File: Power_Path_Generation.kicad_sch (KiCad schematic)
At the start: 8 parts, among them Q602 PMOS SI2365EDS-T1-GE3, U701 TPS7A0233DQNR, U702 TPS3839G33DQNR

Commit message: Added footprints, images, almost finished all èages except for the MCU
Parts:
- added TP701: COUT, 0_Zenith:TestPoint_Pad_D0.5mm_Front, symbol Connector:TestPoint
- added TP702: DOUT, 0_Zenith:TestPoint_Pad_D0.5mm_Front, symbol Connector:TestPoint
- added TP703: -VBAT, 0_Zenith:TestPoint_Pad_D0.5mm_Front, symbol Connector:TestPoint
- added TP704: VBAT, 0_Zenith:TestPoint_Pad_D0.5mm_Front, symbol Connector:TestPoint
- renumbered C616 to C701, C614 to C702, C615 to C703, D602 to D701, Q602 to Q701, R607 to R701, U702 to U701, U701 to U702
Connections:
- net +VBAT: now also TP704.1
- new net -VBAT: TP703.1
- new net COUT: TP701.1
- new net DOUT: TP702.1

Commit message: Added RGB LED, added motor connectors, added test points, imported all 3D models
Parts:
- TP701, TP702, TP703, TP704: footprint 0_Zenith:TestPoint_Pad_D0.5mm_Front -> 0_Plume:TestPoint_Pad_D0.5mm_Back
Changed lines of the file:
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@@
 			"AAAAAAAAAAAAAAAAAAAAAAAAAAAAAAAAAAAAAAAAAAAAAAAAAAAAAAAAAAAAAAAAAAAAAAAAAAAA"
 			"AAAAAAAAAAAAAAAAAAAAAAAAAAAAAAAAAAAAAAAAAAAAAAAAAAAAAAAAAAAAAAAAAAAAAAAAAAAA"
-			"AAAAAAAAAAAAAAAAAAAAAAAAAAAAAAAAAAAAAAAAAAAAAAAAAAAAAAAAAA=="
+			"AAAAAAAAAAAAAAAAAAAAAAAAAAAAAAAAAAAAAAAAAAAAAAAAAAAAAAAAAP//////////////////"
+			"////////////////////////////////////////////////////////////////////////////"
+			"////////////////////////////////////////////////////////////////////////////"
+			"////////////////////////////////////////////////////////////////////////////"
+			"////////////////////////////////////////////////////////////////////////////"
+			"////////////////////////////////////////////////////////////////////////////"
+			"///////////////////////////////+/v7//f39//z8/P/7+/v//Pz8//39/f/+/v7/////////"
+			"///+/v7//Pz8//j3+P/z8/P/7+/v/+fn5//c3Nz/0NDQ/8LCwv+5ubn/tbW1/7Gxsf+tra3/rKys"
+			"/6ysrP+srKz/q6ur/6urq/+rq6v/rKys/62trf+urq7/r6+v/7Gxsf+zs7P/tbW1/7a2tv+4uLj/"
+			"uru5/7y9uv+/v73/wcG//8TDwf/FxML/xsTD/8fGxP/Jx8X/ysjG/8rIxv/JyMb/yMjH/8jIyP/J"
+			"ycn/ycnJ/8rKyv/Ly8v/y8vL/8vLy//My8z/zMzM/8zMzP/MzMz/zc3N/87Ozv/Ozs7/zs7O/87O"
+			"zv/Pz8//z8/P/8/Pz//Pz8//z8/P/8/Pz//Q0ND/0tLR/9PT0f/T09H/09PR/9TU0v/U1NL/1NTS"
+			"/9TU0v/V1dP/1dXT/9XW1P/W19T/1tfU/9bX1P/X19X/19fV/9jX1f/Z19X/2dfV/9nX1f/Z19X/"
+			"2dfV/9nX1f/Z19X/2dfW/9nY1//a2Nf/2tnX/9vZ2P/c2tn/3t3b/97d2//c2tn/2tnX/9nY1v/a"
+			"2Nf/3NvZ/+Df3f/m5eP/5eTi/97d2//g3t3/6ujn/+/t6//v7ev/6ujn/+De3f/Qz87/urq6/6Gh"
+			"of+EhIT/cHBw/2RkZP9bW1v/VVRV/1BQUP9NTU3/SEhI/0NDQ/88PDz/NTU1/zAwMP8vLy//Ly8v"
+			"/zAwMP8wMDD/Ly8v/y8vL/8wMDD/MjIy/zMzM/8zMzP/MjIy/zIyMv8zMzP/MTEx/ywsLP9TU1P/"
+			"qKio/97e3v/09PT//////////////////////////////////v7+//z8/P/7+/v//f39//39/f/9"
+			"/f3//Pz8//n5+f/39/f/9vb2//j4+P/9/f3//v7+//z8/P/4+Pj/8vLy/w=="
 		)
 	)
@@
 			"LoguiC6ILoguiC6ILoguiC6ILoguiC6ILoguiC6ILoguiC6ILoguiC6ILoguiC6ILoguiC6ILogu"
 			"iC6ILoguiC6ILoguiC6ILoguiC6ILoguiC6ILoguiC6ILoguiC6ILoguiC6ILoguiC6ILoguiC6I"
-			"LoguiC6ILg=="
+			"LoguiC6ILmdrQkI0RU5Hb0JBMEgvSUNsT0VMQWdXQmdrQkJvQ0JRRVBqTkkvRDY2Njl2ZnZXTFg2"
+			"MlRaRnRkZmdTM25nbThQQWJVdzFXOEl5TlFKZ2NZUHZSZDJSdXVxVWpySmlUSnNrNUdKeFY1Q1JI"
+			"VFlFc0dKRkloS2U5WjRjOWtSZXp0UjhzVytzbjNIVk1GVzJWYUY2TmVDQm9KRllQQXJ1UG1ZdERn"
+			"bGVVVjNGNVEyRGVvRjdwNElpRkNPVWQ0KzFJMmxmYm9sM0VzV3N6MEU5OW1pTGdsSTJTQ0dwK2Nx"
+			"SVpHSkduNklXY0dPU2JHRFh1RHp0cngwdkpTdEF2RlBvNTJMVUNVMlRvcDVYTWFRTm5kckIveGRk"
+			"ZzdmaVl6N0NMZEYwZGNlaUFXeE11TVE5WUx2Sml6NmJHcEVWamJKcy9INDBReVpLS25OVEZ2VUx6"
+			"bldOR1gvYkZKZ0hnOWo1dHFwdGZjbDFoWjl4ZVZ2RjRKejdRdVhyTytzWUVjTDlmeE9JOGZKQjVy"
+			"a2ViQlhJS2tjc0hCaExscEhXT21KaTFsRFBTOHZiMFo4V2FZUG11cnRjdzZxZEVoWmdqOGJOd1pD"
+			"Ym91cktwMGUzSXVYVjNkUWFaMXM5Y0NKOFdYb1gvV1BEOC9ES01kV013L3oxVzVEVmlzZk1pcTFj"
+			"dzYyeTNPejJESmRCU0JYMGVFRjNIOWU2R3J2bmJ5NDUvN281bS8vdXUvM3REaTdCZmhVNjRWQkFv"
+			"Q0JZR0N3SWVEUUNGb1BoemN5NmdGZ1lKQVFhQWdVQkFvQ1B5V0VUaHd6NEUxVWxjM1VZN0hjVU81"
+			"RjkxMXJMbmRNT29xaHlpNDZ1NVlkYWloUm9CWktwS2lHMFdadXdSemJhSnNhMEZqTmlVVmFlTjRZ"
+			"TVBTSWdhaWNjeEFKVGtyODNFTVNhR3lyYkljbmJQM3Vwc1hhdHp2Nm1xRHBDRW9NR1NBS2JrTkJs"
+			"ekhhb2JzeS9TVm1rbG8yTUsrM2JjVHhOaEM5ZWhmeTR3ZU1rTU5RTVJNUU1yc083QS9YS2Q2K2tu"
+			"UmpCdFZiMThYcEV4dnVGUkpCT25hdE1rOFZuQ3JNU2FPL2FybzZ5NmtXNUlVUThUT1lZd2RXYm5H"
+			"U2NUVENWY2ZaQTh5UUptNDdqdzlUMXVTTlpFbUNPbWNhYTRMa05mU3JKeEp4c3ZqMURhTlo1TkV4"
+			"aWhieHBSSzBYOTJRY3JucWMrRWhmMGtlYlJ5U3ZYei9keTN5eUhoNGZqZVM2NVlpZlRhV3plVE5z"
+			"N0o2MGlvWUR2WStDeHdoWHZlWjExNFZqbzZKSTNzczZwR0ljZEd4MFo0YmlCajFwZHB4N2pFRFZy"
+			"RGNtWmJVbw=="
 		)
 	)
@@
 			)
 		)
-		(property "Datasheet" "https://www.mouser.ch/ProductDetail/Panasonic/ERJ-2RKF1003X?qs=H7k1u0Mp9JQnXoBKdf15Qg%3D%3D&utm_id=9873308309&utm_source=google&utm_medium=cpc&utm_marketing_tactic=emeacorp&gad_source=1&gbraid=0AAAAADn_wf3ug0UXYvYZGGeVkpnwzKIx2&gclid=CjwKCAjw7pO_BhAlEiwA4pMQvN26O09RJza20J-tNmeCWzVs5ziPoEm0EaMPJxUJNGkJ9vP3fDT5GRoCNbIQAvD_BwE"
+		(property "Datasheet" "~"
 			(at 105.41 101.6 0)
 			(effects
@@
 			)
 		)
-		(property "Datasheet" "https://www.mouser.ch/ProductDetail/Samsung-Electro-Mechanics/CL05B104KO5VPNC?qs=SRYZG9HaIQ0dGqjRr5dbew%3D%3D&srsltid=AfmBOopjHQwv3QSXf_w3_Ogf1nZFnivKZ-jQ4-9snVp7pU9kKH2s_vpO"
+		(property "Datasheet" "~"
 			(at 160.02 95.25 0)
 			(effects
@@
 			)
 		)
-		(property "Datasheet" "https://www.mouser.ch/ProductDetail/Murata-Electronics/GRM188R61C106MAALD?qs=hNud%2FORuBR3LEOKZ4RJp9w%3D%3D"
+		(property "Datasheet" "~"
 			(at 193.04 114.3 0)
 			(effects
@@
 			)
 		)
-		(property "Datasheet" "https://www.mouser.ch/ProductDetail/TDK/CGA3E1X7R1C105K080AC?qs=XHchNesRtUbBVNsGg9%252BP9g%3D%3D"
+		(property "Datasheet" "~"
 			(at 162.56 114.3 0)
 			(effects
@@
 			)
 		)
-		(property "Footprint" "0_Zenith:TestPoint_Pad_D0.5mm_Front"
+		(property "Footprint" "0_Plume:TestPoint_Pad_D0.5mm_Back"
 			(at 46.99 163.83 0)
 			(effects
@@
 		)
 		(property "Supplier" ""
-			(at 46.99 168.91 0)
-			(effects
-				(font
-					(size 1.27 1.27)
-				)
-				(hide yes)
-			)
-		)
-		(property "LCSC Part #" "~"
 			(at 46.99 168.91 0)
 			(effects
@@
 			)
 		)
-		(property "Footprint" "0_Zenith:TestPoint_Pad_D0.5mm_Front"
+		(property "Footprint" "0_Plume:TestPoint_Pad_D0.5mm_Back"
 			(at 46.99 168.91 0)
 			(effects
@@
 		)
 		(property "Supplier" ""
-			(at 46.99 173.99 0)
-			(effects
-				(font
-					(size 1.27 1.27)
-				)
-				(hide yes)
-			)
-		)
-		(property "LCSC Part #" "~"
 			(at 46.99 173.99 0)
 			(effects
@@
 			)
 		)
-		(property "Footprint" "0_Zenith:TestPoint_Pad_D0.5mm_Front"
+		(property "Footprint" "0_Plume:TestPoint_Pad_D0.5mm_Back"
 			(at 46.99 158.75 0)
 			(effects
@@
 		)
 		(property "Supplier" ""
-			(at 46.99 163.83 0)
-			(effects
-				(font
-					(size 1.27 1.27)
-				)
-				(hide yes)
-			)
-		)
-		(property "LCSC Part #" "~"
 			(at 46.99 163.83 0)
 			(effects
@@
 			)
 		)
-		(property "Datasheet" "https://assets.nexperia.com/documents/data-sheet/PMEG60T20ELR.pdf"
+		(property "Datasheet" "~"
 			(at 124.46 102.87 0)
 			(effects
@@
 			)
 		)
-		(property "Footprint" "0_Zenith:TestPoint_Pad_D0.5mm_Front"
+		(property "Footprint" "0_Plume:TestPoint_Pad_D0.5mm_Back"
 			(at 46.99 153.67 0)
 			(effects
@@
 			(at 46.99 158.75 0)
 			(effects
-				(font
-					(size 1.27 1.27)
-				)
-				(hide yes)
-			)
-		)
-		(property "LCSC Part #" "~"
-			(at 46.99 158.75 0)
-			(effects

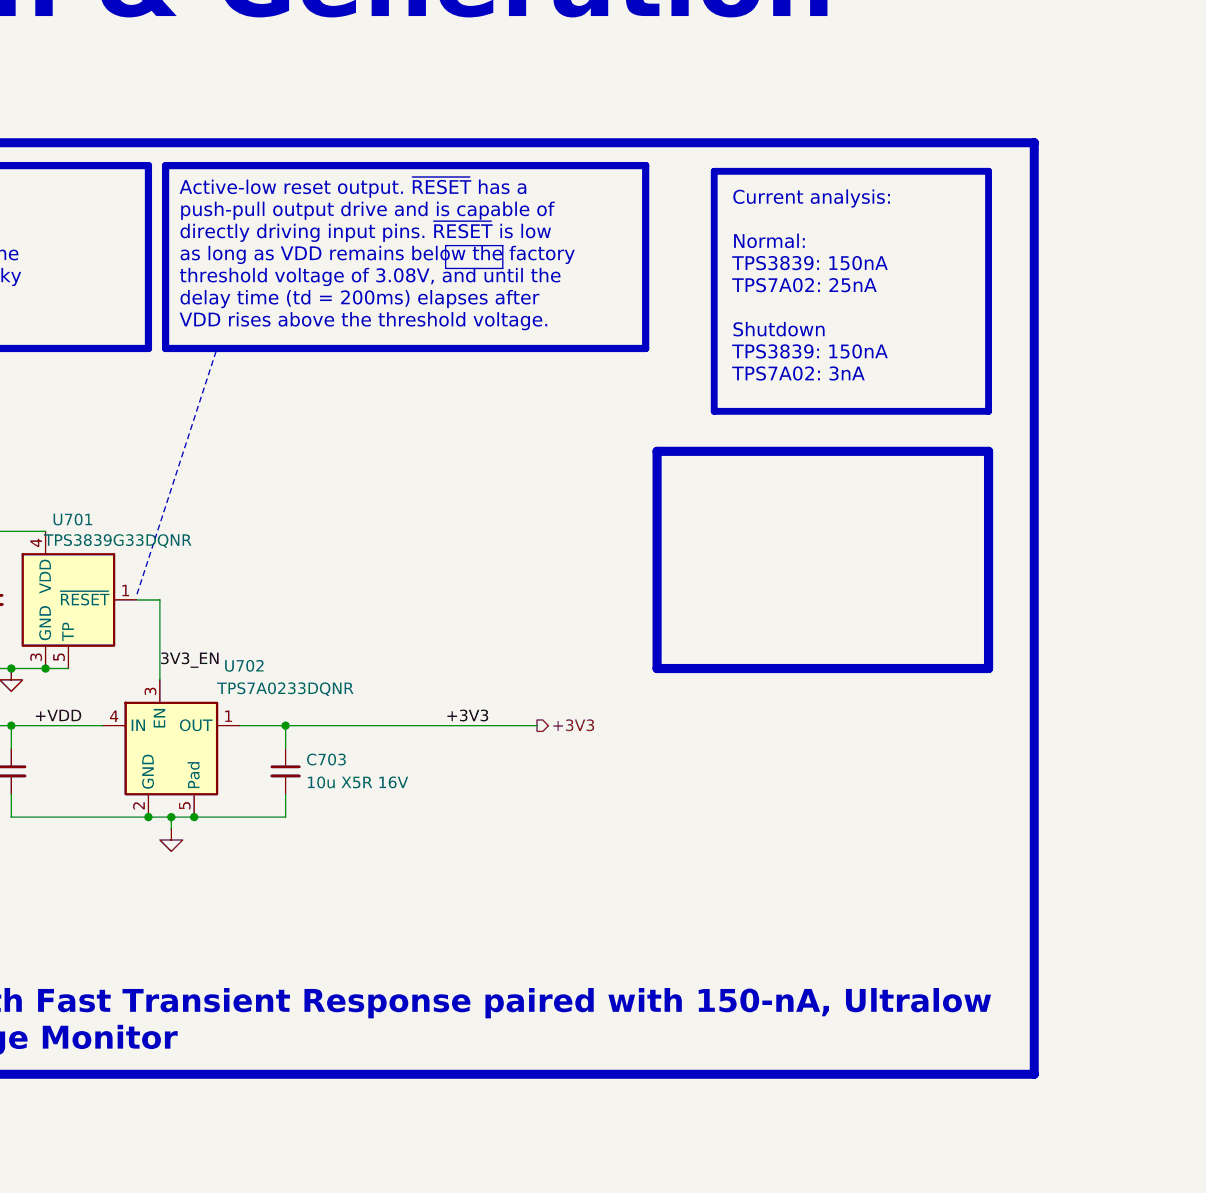
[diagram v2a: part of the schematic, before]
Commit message: Finished schematic, imported all footprints, all 3D models and created STM32 project, now need to proofread shematic before layout
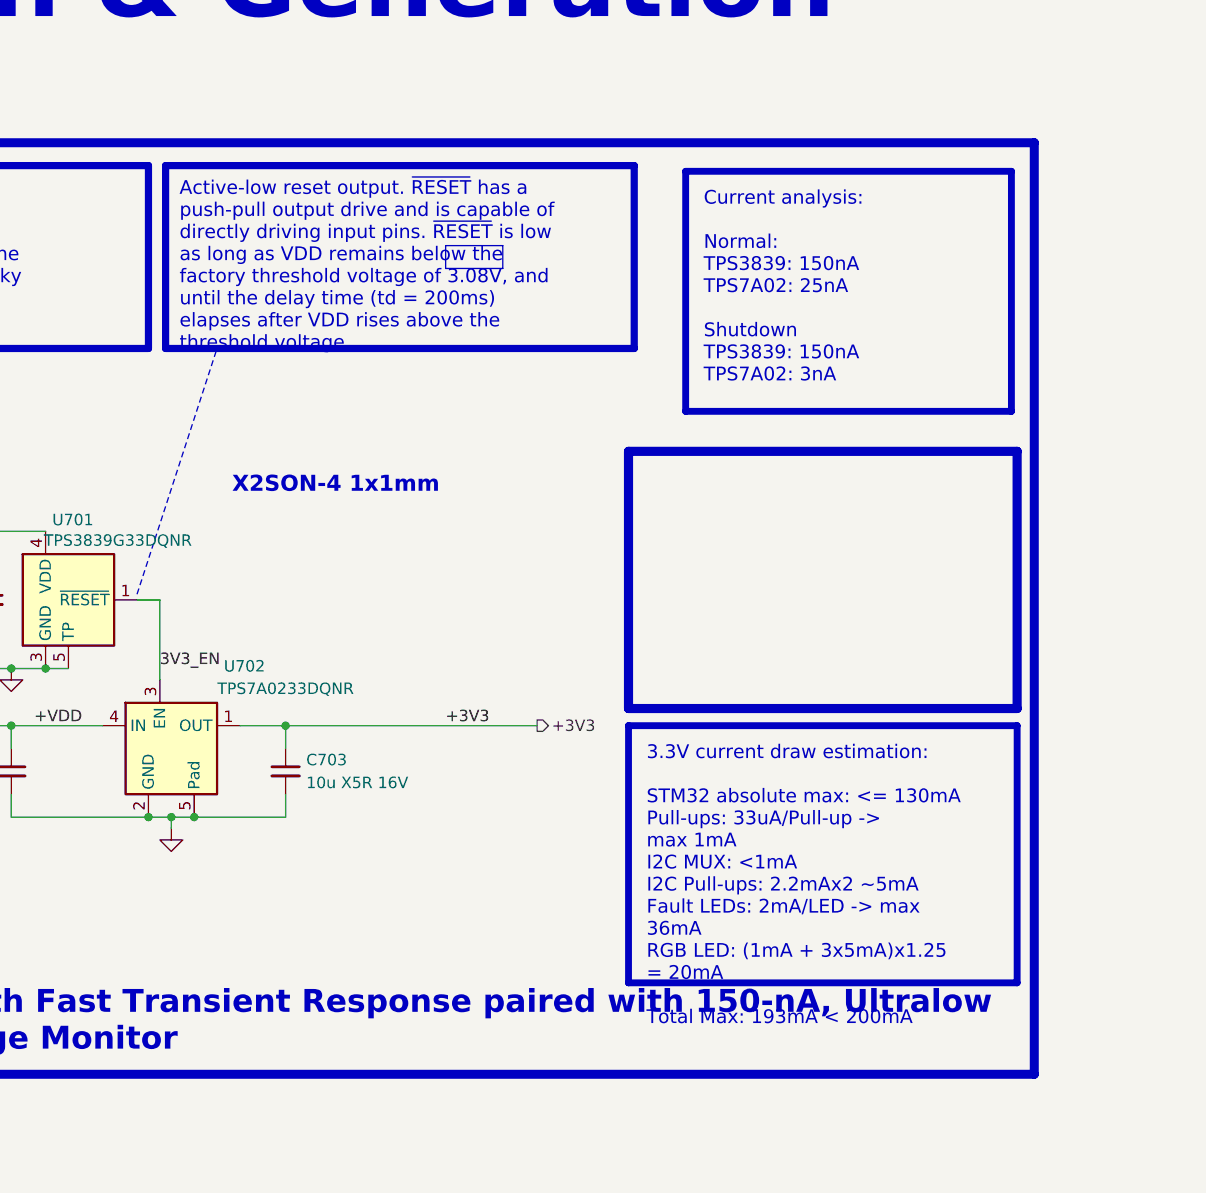
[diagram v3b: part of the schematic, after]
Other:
- note added: "X2SON-4 1x1mm"
